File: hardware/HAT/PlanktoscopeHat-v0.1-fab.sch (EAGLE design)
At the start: 90 parts, among them K1 PINHD-2X20, P4 MA08-1, P5 MA08-1, P6 MA02-1, P7 MA08-1, P8 MA08-1, P9 MA02-1, Q1 5.8A/30V/35mΩ, Q2 DMG2305UX, Q3 DMP3013SFV-7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

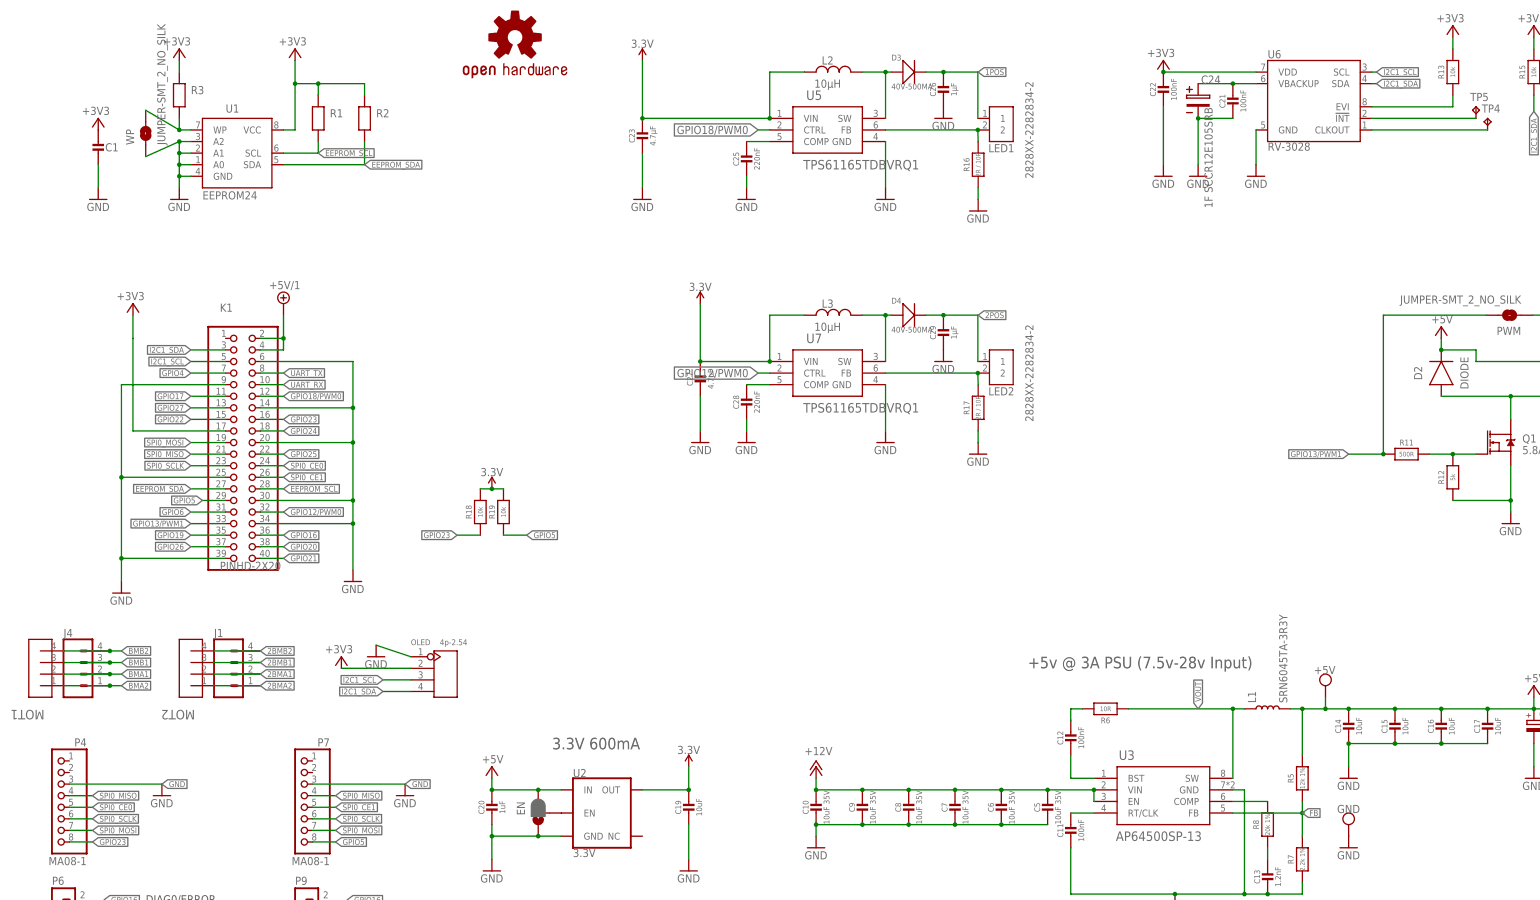
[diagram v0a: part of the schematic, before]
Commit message: Hardware: BOM Addition and schematic update
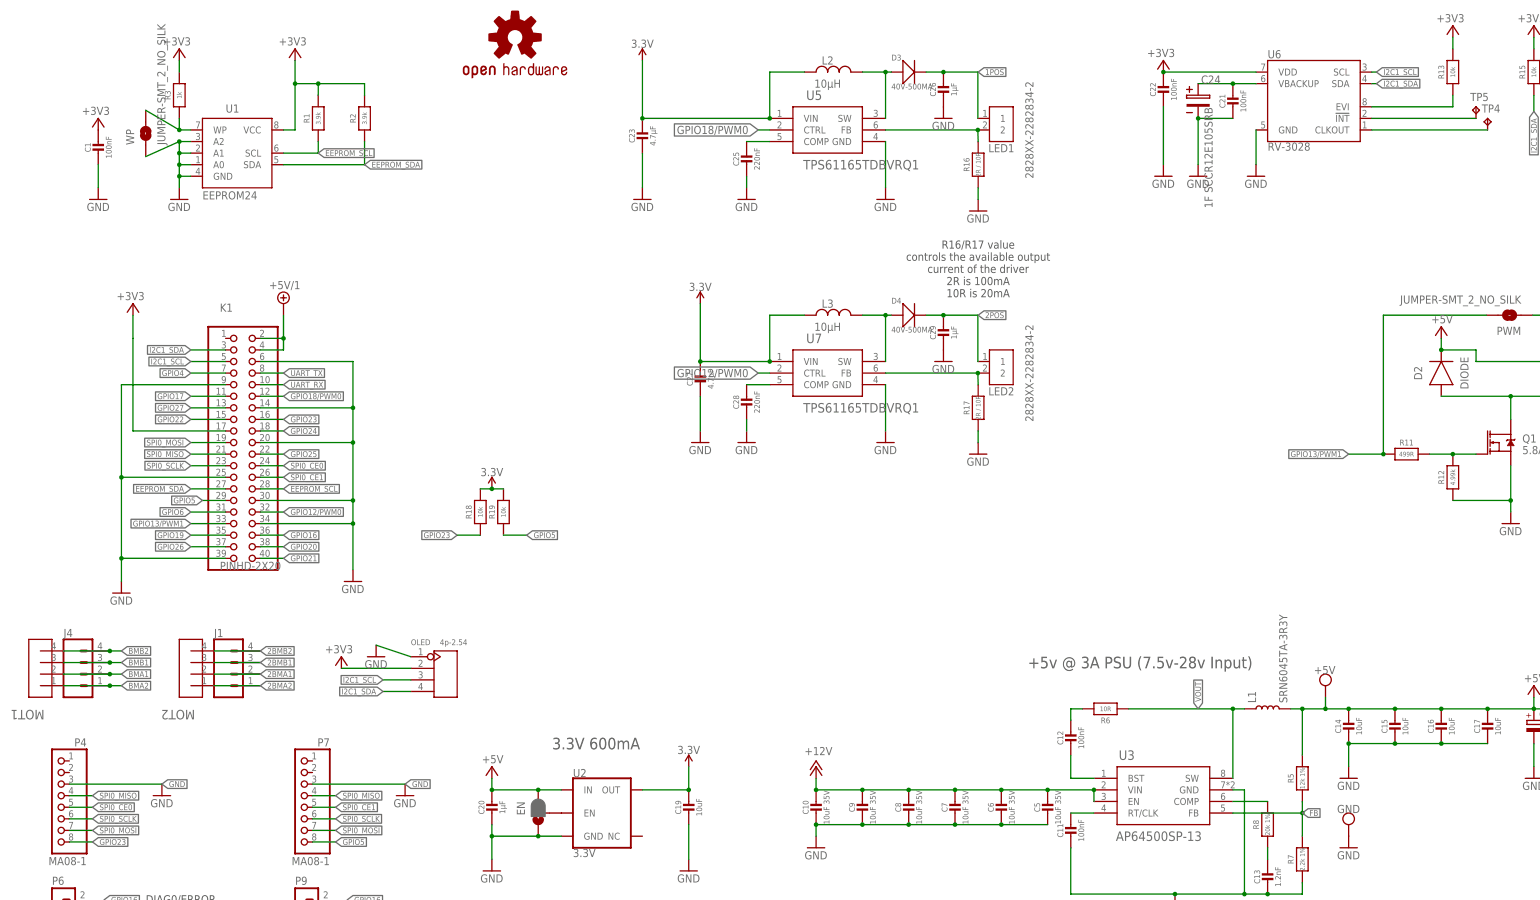
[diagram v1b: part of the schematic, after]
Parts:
- C20: value 1uF -> 1µF
- R11: value 500R -> 499R
- R12: value 5k -> 4.99k
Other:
- note added: "R16/R17 value controls the available output current of the driver 2R is 100mA 10R is 20mA"
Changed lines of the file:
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@@
 <part name="WP" library="SparkFun-Jumpers" library_urn="urn:adsk.eagle:library:528" deviceset="JUMPER-SMT_2_NO" device="_SILK" package3d_urn="urn:adsk.eagle:package:39279/1"/>
 <part name="C19" library="microbuilder" library_urn="urn:adsk.eagle:library:18156183" deviceset="CAP_CERAMIC" device="_0805MP" package3d_urn="urn:adsk.eagle:package:18156346/1" value="10uF"/>
-<part name="C20" library="microbuilder" library_urn="urn:adsk.eagle:library:18156183" deviceset="CAP_CERAMIC" device="_0805MP" package3d_urn="urn:adsk.eagle:package:18156346/1" value="1uF"/>
+<part name="C20" library="microbuilder" library_urn="urn:adsk.eagle:library:18156183" deviceset="CAP_CERAMIC" device="_0805MP" package3d_urn="urn:adsk.eagle:package:18156346/1" value="1µF"/>
 <part name="EN" library="SparkFun-Jumpers" library_urn="urn:adsk.eagle:library:528" deviceset="JUMPER-SMT_3_1-NC_PASTE" device="_SILK" package3d_urn="urn:adsk.eagle:package:39293/1"/>
 <part name="GND18" library="supply1" library_urn="urn:adsk.eagle:library:371" deviceset="GND" device=""/>
 <part name="MOT1" library="PScope" deviceset="S4B-XH-SM4-TB(LF)(SN)" device=""/>
 <part name="MOT2" library="PScope" deviceset="S4B-XH-SM4-TB(LF)(SN)" device=""/>
-<part name="R11" library="microbuilder" library_urn="urn:adsk.eagle:library:18156183" deviceset="RESISTOR" device="_0805MP" package3d_urn="urn:adsk.eagle:package:18156346/1" value="500R"/>
-<part name="R12" library="microbuilder" library_urn="urn:adsk.eagle:library:18156183" deviceset="RESISTOR" device="_0805MP" package3d_urn="urn:adsk.eagle:package:18156346/1" value="5k"/>
+<part name="R11" library="microbuilder" library_urn="urn:adsk.eagle:library:18156183" deviceset="RESISTOR" device="_0805MP" package3d_urn="urn:adsk.eagle:package:18156346/1" value="499R"/>
+<part name="R12" library="microbuilder" library_urn="urn:adsk.eagle:library:18156183" deviceset="RESISTOR" device="_0805MP" package3d_urn="urn:adsk.eagle:package:18156346/1" value="4.99k"/>
 <part name="D2" library="Diode" library_urn="urn:adsk.eagle:library:16378169" deviceset="DIODE" device="DO-214AC(SMA)" package3d_urn="urn:adsk.eagle:package:16378188/1" value="DIODE"/>
 <part name="GND19" library="supply1" library_urn="urn:adsk.eagle:library:371" deviceset="GND" device=""/>
@@
 <text x="30.734" y="51.308" size="1.778" layer="97">DIAG0/ERROR</text>
 <text x="30.734" y="48.768" size="1.778" layer="97">DIAG1/STALL</text>
+<text x="213.36" y="190.5" size="1.778" layer="97" align="center">R16/R17 value
+controls the available output
+current of the driver
+2R is 100mA
+10R is 20mA</text>
 </plain>
 <instances>
@@
 </instance>
 <instance part="R1" gate="G$1" x="68.58" y="223.52" smashed="yes" rot="R90">
-<attribute name="NAME" x="71.12" y="223.7486" size="1.778" layer="95"/>
+<attribute name="NAME" x="66.04" y="223.52" size="1.27" layer="95" font="vector" rot="R90" align="center"/>
+<attribute name="VALUE" x="68.58" y="223.52" size="1.016" layer="96" font="vector" ratio="15" rot="R90" align="center"/>
 </instance>
 <instance part="+3V10" gate="G$1" x="63.5" y="238.76" smashed="yes">
@@
 <instance part="C1" gate="G$1" x="20.32" y="215.9" smashed="yes">
 <attribute name="DIELECTRIC" x="20.32" y="215.9" size="1.778" layer="96" display="off"/>
-<attribute name="NAME" x="21.844" y="216.281" size="1.778" layer="95"/>
+<attribute name="NAME" x="18.03" y="217.15" size="1.27" layer="95" font="vector" rot="R90" align="center"/>
+<attribute name="VALUE" x="22.62" y="217.15" size="1.27" layer="96" font="vector" rot="R90" align="center"/>
 </instance>
 <instance part="R2" gate="G$1" x="78.74" y="223.52" smashed="yes" rot="R90">
-<attribute name="NAME" x="81.28" y="223.7486" size="1.778" layer="95"/>
+<attribute name="NAME" x="76.2" y="223.52" size="1.27" layer="95" font="vector" rot="R90" align="center"/>
+<attribute name="VALUE" x="78.74" y="223.52" size="1.016" layer="96" font="vector" ratio="15" rot="R90" align="center"/>
 </instance>
 <instance part="R3" gate="G$1" x="38.1" y="228.6" smashed="yes" rot="R90">
-<attribute name="NAME" x="40.64" y="228.8286" size="1.778" layer="95"/>
+<attribute name="NAME" x="35.56" y="228.6" size="1.27" layer="95" font="vector" rot="R90" align="center"/>
+<attribute name="VALUE" x="38.1" y="228.6" size="1.016" layer="96" font="vector" ratio="15" rot="R90" align="center"/>
 </instance>
 <instance part="+3V4" gate="G$1" x="38.1" y="238.76" smashed="yes">
@@
 </drawing>
 <compatibility>
+<note version="6.3" minversion="6.2.2" severity="warning">
+Since Version 6.2.2 text objects can contain more than one line,
+which will not be processed correctly with this version.
+</note>
 <note version="8.2" severity="warning">
 Since Version 8.2, EAGLE supports online libraries. The ids

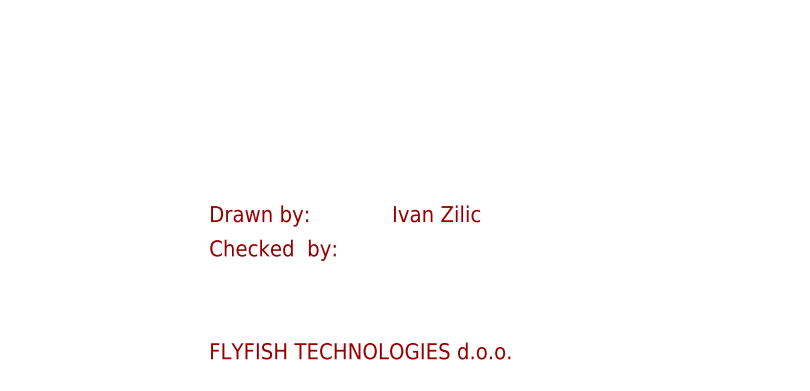
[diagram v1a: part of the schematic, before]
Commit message: hardware: update schematics note block and add pdf
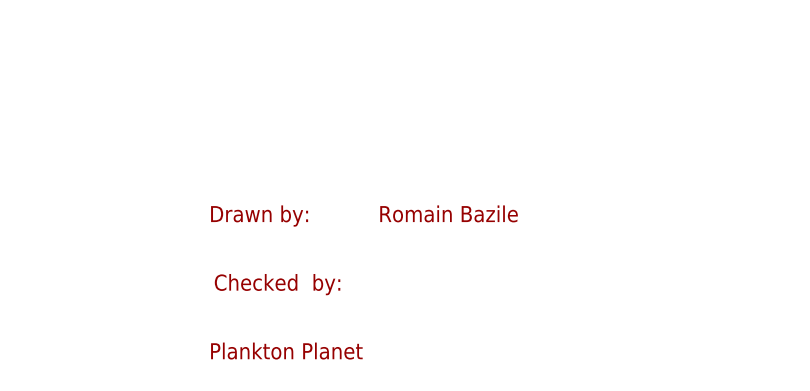
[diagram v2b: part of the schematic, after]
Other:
- note added: "Plankton Planet"
- note added: "Romain Bazile"
- note removed: "FLYFISH TECHNOLOGIES d.o.o."
- note removed: "Ivan Zilic"
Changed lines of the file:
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@@
 <plain>
 <text x="289.56" y="20.32" size="1.778" layer="94" ratio="15">Drawn by:</text>
-<text x="289.56" y="16.51" size="1.778" layer="94" ratio="15">Checked  by:</text>
-<text x="289.56" y="5.08" size="1.778" layer="94">FLYFISH TECHNOLOGIES d.o.o.</text>
-<text x="309.88" y="20.32" size="1.778" layer="94">Ivan Zilic</text>
+<text x="290.068" y="12.7" size="1.778" layer="94" ratio="15">Checked  by:</text>
+<text x="289.56" y="5.08" size="1.778" layer="94">Plankton Planet</text>
+<text x="308.356" y="20.32" size="1.778" layer="94">Romain Bazile</text>
 <text x="374.65" y="5.08" size="2.54" layer="94" ratio="10">v0.1</text>
 <wire x1="353.06" y1="104.14" x2="355.6" y2="104.14" width="0.1524" layer="97"/>
